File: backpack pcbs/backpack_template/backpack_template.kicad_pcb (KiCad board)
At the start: 2 copper layers, 30 x 22.5 mm, 9 parts

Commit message: Backpack changes
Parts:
- removed the REF** at (163.1, 87.4)
- removed the REF** at (189.0, 87.4)
- added REF**: PinHeader_1x08_P2.54mm_Vertical, Connector_PinHeader_2.54mm:PinHeader_1x08_P2.54mm_Vertical, B.Cu at (189.5, 56.1)
- added REF**: PinHeader_1x08_P2.54mm_Vertical, Connector_PinHeader_2.54mm:PinHeader_1x08_P2.54mm_Vertical, B.Cu at (162.0, 56.1)
- moved REF** 31.3 mm to (167.4, 73.6)
- moved REF** 31.3 mm to (170.7, 74.2)
- moved REF** 31.3 mm to (184.2, 73.6)
- moved REF** 31.0 mm to (177.8, 71.4)
- moved REF** 31.0 mm to (173.7, 71.4)
- moved REF** 30.5 mm to (170.2, 71.4)
- moved REF** 30.3 mm to (181.4, 71.4)
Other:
- board text added: "blue"
- board text added: "gnd"
- board text added: "green/led"
- board text added: "red"
- board text added: "x"
- board text added: "x1"
- board text added: "x2"
- board text added: "x3"
- board text added: "x4"
- board text added: "y"
- board text added: "y1"
- board text added: "y2"
- board text added: "y3"
- board text added: "y4"
- board text added: "z"
- board text added: "z1"
- board text added: "z2"
- board text added: "z3"
- board text added: "z4"

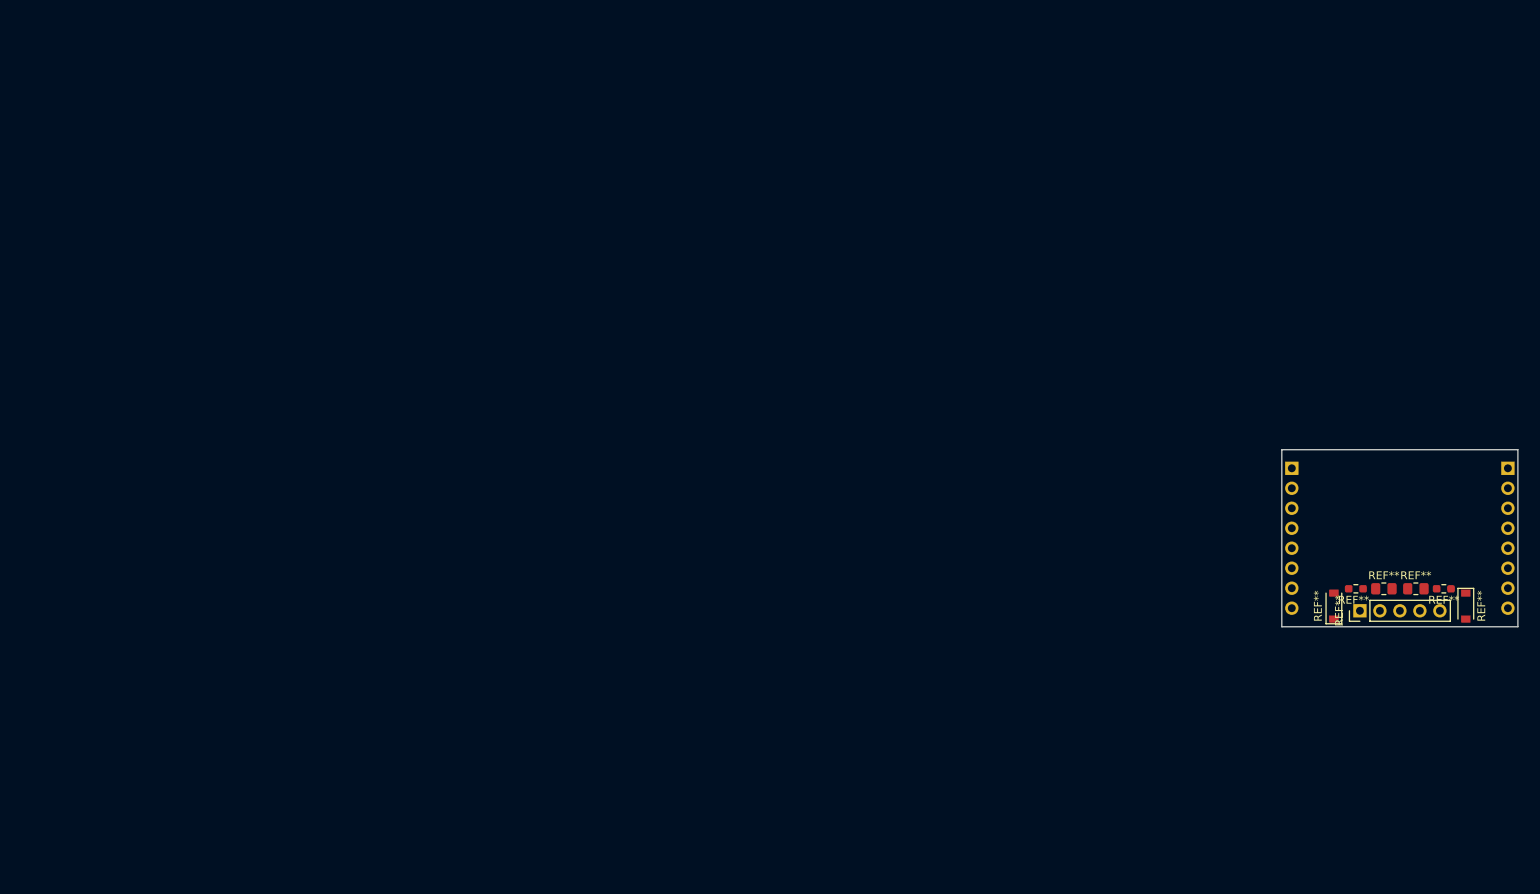
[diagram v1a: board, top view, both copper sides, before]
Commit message: Backpack template PCB changes
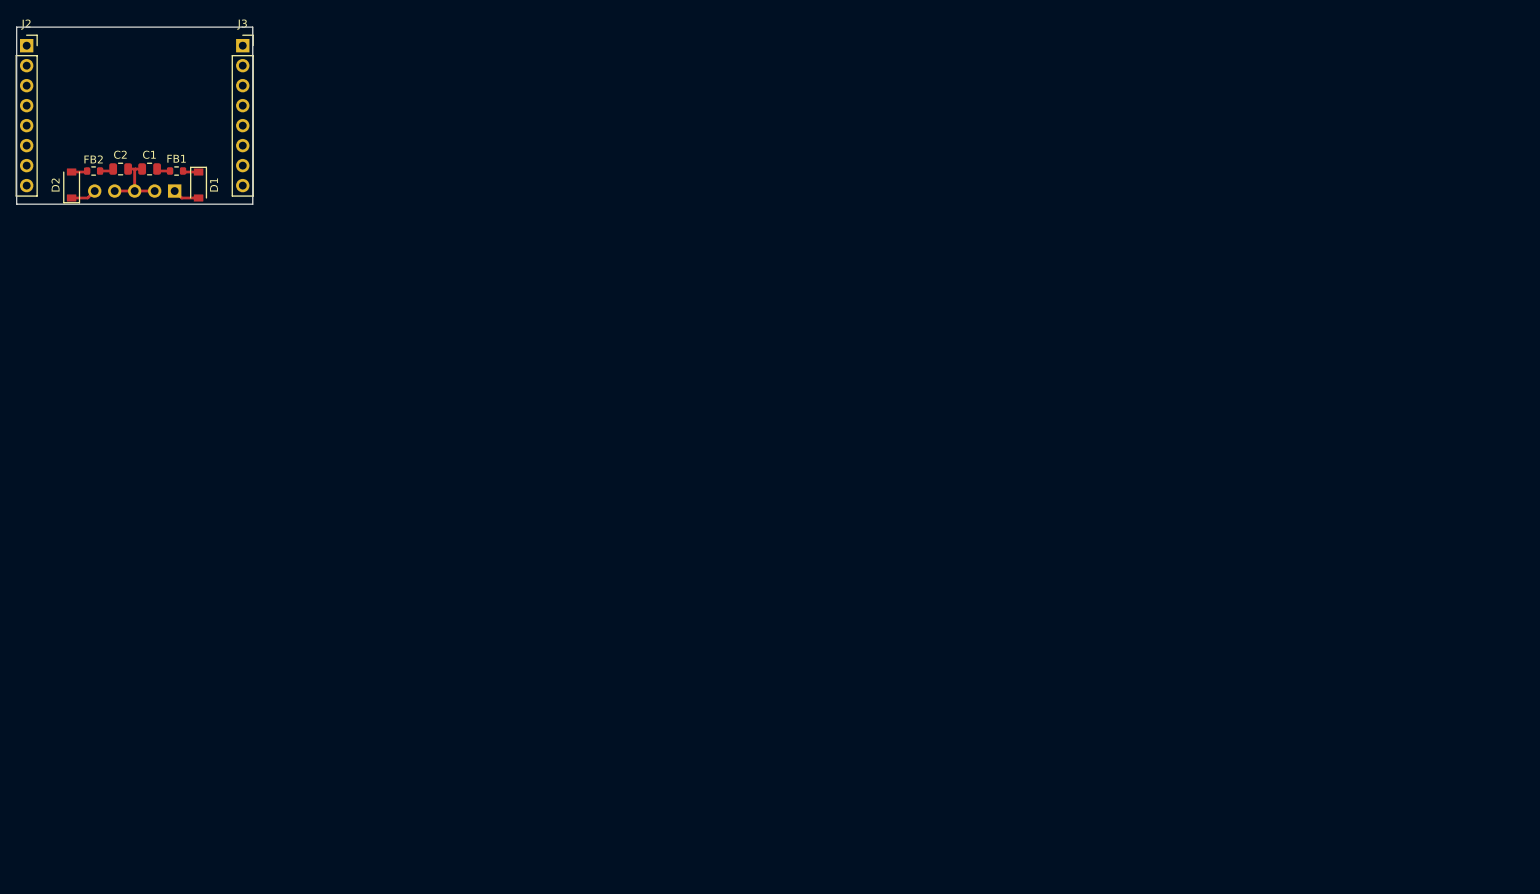
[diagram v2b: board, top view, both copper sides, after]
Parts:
- removed REF** (x2): R_0603_1608Metric_Pad0.98x0.95mm_HandSolder, Resistor_SMD:R_0603_1608Metric_Pad0.98x0.95mm_HandSolder
- removed REF** (x2): C_0805_2012Metric_Pad1.18x1.45mm_HandSolder, Capacitor_SMD:C_0805_2012Metric_Pad1.18x1.45mm_HandSolder
- removed REF** (x2): D_SOD-123, Diode_SMD:D_SOD-123
- removed REF**: PinHeader_1x05_P2.54mm_Vertical, Connector_PinHeader_2.54mm:PinHeader_1x05_P2.54mm_Vertical
- removed REF** (x2): PinHeader_1x08_P2.54mm_Vertical, Connector_PinHeader_2.54mm:PinHeader_1x08_P2.54mm_Vertical
- added C1: 10uF, Capacitor_SMD:C_0805_2012Metric, F.Cu at (16.9, 18.0)
- added C2: 10uF, Capacitor_SMD:C_0805_2012Metric, F.Cu at (13.2, 18.0)
- added D1: 1N5817, Diode_SMD:D_SOD-123, F.Cu at (23.1, 20.1)
- added D2: 1N5817, Diode_SMD:D_SOD-123, F.Cu at (6.99, 20.1)
- added FB1: FerriteBead_Small, Resistor_SMD:R_0603_1608Metric, F.Cu at (20.3, 18.3)
- added FB2: FerriteBead_Small, Resistor_SMD:R_0603_1608Metric, F.Cu at (9.78, 18.3)
- added J1: Conn_01x05_Male, Connector_PinHeader_2.54mm:PinHeader_1x05_P2.54mm_Vertical, B.Cu at (20.1, 20.8)
- added J2: Conn_01x08_Female, Connector_PinSocket_2.54mm:PinSocket_1x08_P2.54mm_Vertical, F.Cu at (1.27, 2.36)
- added J3: Conn_01x08_Female, Connector_PinSocket_2.54mm:PinSocket_1x08_P2.54mm_Vertical, F.Cu at (28.7, 2.36)
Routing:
- net GND: track 0.00 -> 9.70 mm
- net Net-(D1-Pad2): track 0.00 -> 3.40 mm
- net Net-(D2-Pad1): track 0.00 -> 3.30 mm
- net Net-(D1-Pad1): track 0.00 -> 2.02 mm
- net Net-(D2-Pad2): track 0.00 -> 2.02 mm
- net -12V: track 0.00 -> 1.76 mm
- net +12V: track 0.00 -> 1.76 mm
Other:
- board text added: "-12V!"
- board text removed: "x1"
- board text removed: "x2"
- board text removed: "x3"
- board text removed: "x4"
- board text removed: "y1"
- board text removed: "y2"
- board text removed: "y3"
- board text removed: "y4"
- board text removed: "z1"
- board text removed: "z2"
- board text removed: "z3"
- board text removed: "z4"

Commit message: KiCad Save
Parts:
- moved C1 1.00 mm to (16.9, 17.0)
- moved C2 1.00 mm to (13.2, 17.0)
- moved D1 1.00 mm to (23.1, 19.1)
- moved D2 1.00 mm to (6.99, 19.1)
- moved FB1 1.00 mm to (20.3, 17.3)
- moved FB2 1.00 mm to (9.78, 17.3)
- moved J1 1.00 mm to (20.1, 19.8)
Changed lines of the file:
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@@
   (net 23 "unconnected-(J3-Pad8)")
   (footprint "Resistor_SMD:R_0603_1608Metric" (layer "F.Cu")
-    (at 20.32 18.288 180)
+    (at 20.325 17.291 180)
     (descr "Resistor SMD 0603 (1608 Metric), square (rectangular) end terminal, IPC_7351 nominal, (Body size source: IPC-SM-782 page 72, https://www.pcb-3d.com/wordpress/wp-content/uploads/ipc-sm-782a_amendment_1_and_2.pdf), generated with kicad-footprint-generator")
     (tags "resistor")
@@
   )
   (footprint "Diode_SMD:D_SOD-123" (layer "F.Cu")
-    (at 6.985 20.066 90)
+    (at 6.99 19.069 90)
     (descr "SOD-123")
     (tags "SOD-123")
@@
   )
   (footprint "Capacitor_SMD:C_0805_2012Metric" (layer "F.Cu")
-    (at 16.891 18.034 180)
+    (at 16.896 17.037 180)
     (descr "Capacitor SMD 0805 (2012 Metric), square (rectangular) end terminal, IPC_7351 nominal, (Body size source: IPC-SM-782 page 76, https://www.pcb-3d.com/wordpress/wp-content/uploads/ipc-sm-782a_amendment_1_and_2.pdf, https://docs.google.com/spreadsheets/d/1BsfQQcO9C6DZCsRaXUlFlo91Tg2WpOkGARC1WS5S8t0/edit?usp=sharing), generated with kicad-footprint-generator")
     (tags "capacitor")
@@
   )
   (footprint "Resistor_SMD:R_0603_1608Metric" (layer "F.Cu")
-    (at 9.779 18.288)
+    (at 9.784 17.291)
     (descr "Resistor SMD 0603 (1608 Metric), square (rectangular) end terminal, IPC_7351 nominal, (Body size source: IPC-SM-782 page 72, https://www.pcb-3d.com/wordpress/wp-content/uploads/ipc-sm-782a_amendment_1_and_2.pdf), generated with kicad-footprint-generator")
     (tags "resistor")
@@
   )
   (footprint "Diode_SMD:D_SOD-123" (layer "F.Cu")
-    (at 23.114 20.066 -90)
+    (at 23.119 19.069 -90)
     (descr "SOD-123")
     (tags "SOD-123")
@@
   )
   (footprint "Capacitor_SMD:C_0805_2012Metric" (layer "F.Cu")
-    (at 13.208 18.034 180)
+    (at 13.213 17.037 180)
     (descr "Capacitor SMD 0805 (2012 Metric), square (rectangular) end terminal, IPC_7351 nominal, (Body size source: IPC-SM-782 page 76, https://www.pcb-3d.com/wordpress/wp-content/uploads/ipc-sm-782a_amendment_1_and_2.pdf, https://docs.google.com/spreadsheets/d/1BsfQQcO9C6DZCsRaXUlFlo91Tg2WpOkGARC1WS5S8t0/edit?usp=sharing), generated with kicad-footprint-generator")
     (tags "capacitor")
@@
   )
   (footprint "Connector_PinHeader_2.54mm:PinHeader_1x05_P2.54mm_Vertical" (layer "B.Cu")
-    (at 20.08 20.828 90)
+    (at 20.085 19.831 90)
     (descr "Through hole straight pin header, 1x05, 2.54mm pitch, single row")
     (tags "Through hole pin header THT 1x05 2.54mm single row")
@@
   )
   (target plus (at 0 0) (size 5) (width 0.1) (layer "Edge.Cuts"))
-  (segment (start 19.495 18.288) (end 18.095 18.288) (width 0.35) (layer "F.Cu") (net 1))
-  (segment (start 18.095 18.288) (end 17.841 18.034) (width 0.35) (layer "F.Cu") (net 1))
-  (segment (start 15 20.828) (end 15 18.147) (width 0.35) (layer "F.Cu") (net 2))
-  (segment (start 15 18.147) (end 15.113 18.034) (width 0.35) (layer "F.Cu") (net 2))
-  (segment (start 12.46 20.828) (end 17.54 20.828) (width 0.35) (layer "F.Cu") (net 2))
-  (segment (start 14.158 18.034) (end 15.113 18.034) (width 0.35) (layer "F.Cu") (net 2))
-  (segment (start 15.113 18.034) (end 15.941 18.034) (width 0.35) (layer "F.Cu") (net 2))
-  (segment (start 12.004 18.288) (end 12.258 18.034) (width 0.35) (layer "F.Cu") (net 3))
-  (segment (start 10.604 18.288) (end 12.004 18.288) (width 0.35) (layer "F.Cu") (net 3))
-  (segment (start 21.273 18.416) (end 21.145 18.288) (width 0.35) (layer "F.Cu") (net 4))
-  (segment (start 23.114 18.416) (end 21.273 18.416) (width 0.35) (layer "F.Cu") (net 4))
-  (segment (start 20.968 21.716) (end 20.08 20.828) (width 0.35) (layer "F.Cu") (net 5))
-  (segment (start 23.114 21.716) (end 20.968 21.716) (width 0.35) (layer "F.Cu") (net 5))
-  (segment (start 6.985 21.716) (end 9.032 21.716) (width 0.35) (layer "F.Cu") (net 6))
-  (segment (start 9.032 21.716) (end 9.92 20.828) (width 0.35) (layer "F.Cu") (net 6))
-  (segment (start 8.826 18.416) (end 8.954 18.288) (width 0.35) (layer "F.Cu") (net 7))
-  (segment (start 6.985 18.416) (end 8.826 18.416) (width 0.35) (layer "F.Cu") (net 7))
+  (segment (start 19.5 17.291) (end 18.1 17.291) (width 0.35) (layer "F.Cu") (net 1))
+  (segment (start 18.1 17.291) (end 17.846 17.037) (width 0.35) (layer "F.Cu") (net 1))
+  (segment (start 15.005 19.831) (end 15.005 17.15) (width 0.35) (layer "F.Cu") (net 2))
+  (segment (start 15.005 17.15) (end 15.118 17.037) (width 0.35) (layer "F.Cu") (net 2))
+  (segment (start 12.465 19.831) (end 17.545 19.831) (width 0.35) (layer "F.Cu") (net 2))
+  (segment (start 14.163 17.037) (end 15.118 17.037) (width 0.35) (layer "F.Cu") (net 2))
+  (segment (start 15.118 17.037) (end 15.946 17.037) (width 0.35) (layer "F.Cu") (net 2))
+  (segment (start 12.009 17.291) (end 12.263 17.037) (width 0.35) (layer "F.Cu") (net 3))
+  (segment (start 10.609 17.291) (end 12.009 17.291) (width 0.35) (layer "F.Cu") (net 3))
+  (segment (start 21.278 17.419) (end 21.15 17.291) (width 0.35) (layer "F.Cu") (net 4))
+  (segment (start 23.119 17.419) (end 21.278 17.419) (width 0.35) (layer "F.Cu") (net 4))
+  (segment (start 20.973 20.719) (end 20.085 19.831) (width 0.35) (layer "F.Cu") (net 5))
+  (segment (start 23.119 20.719) (end 20.973 20.719) (width 0.35) (layer "F.Cu") (net 5))
+  (segment (start 6.99 20.719) (end 9.037 20.719) (width 0.35) (layer "F.Cu") (net 6))
+  (segment (start 9.037 20.719) (end 9.925 19.831) (width 0.35) (layer "F.Cu") (net 6))
+  (segment (start 8.831 17.419) (end 8.959 17.291) (width 0.35) (layer "F.Cu") (net 7))
+  (segment (start 6.99 17.419) (end 8.831 17.419) (width 0.35) (layer "F.Cu") (net 7))
   (zone (net 0) (net_name "") (layer "B.SilkS") (hatch none 0.508)
     (connect_pads (clearance 0.508))
